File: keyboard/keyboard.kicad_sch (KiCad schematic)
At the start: 4 parts

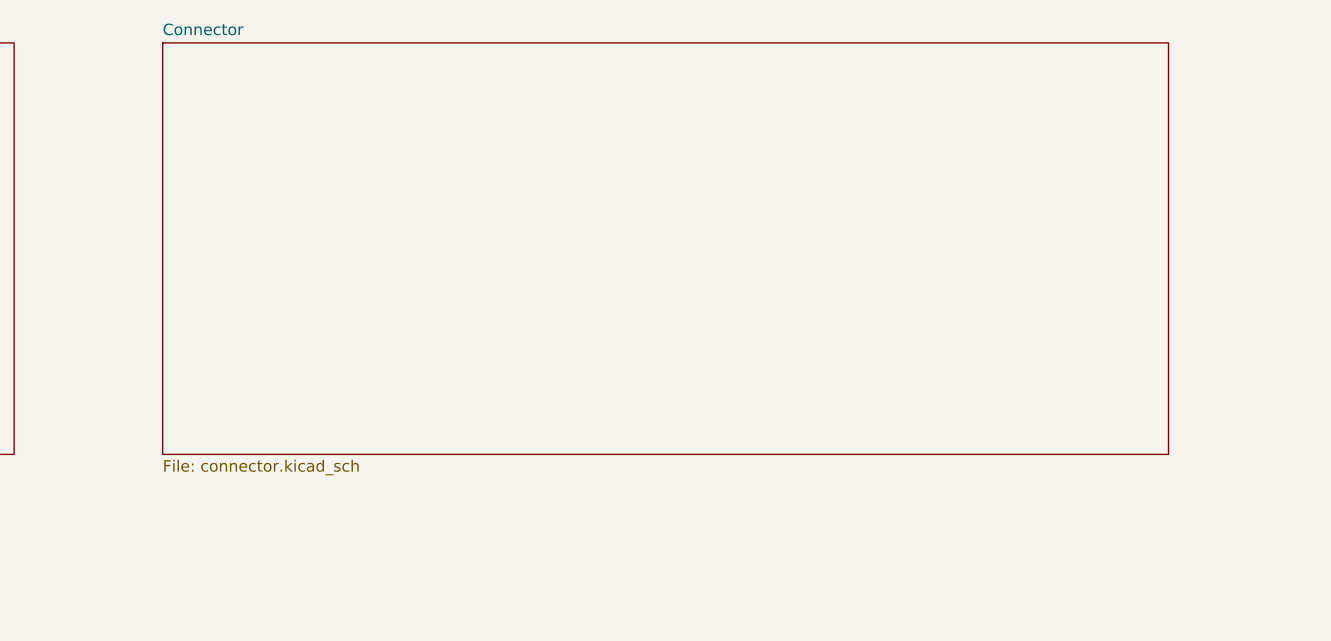
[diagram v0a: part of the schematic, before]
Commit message: Add 3dshapes, footprint library, symbol library, and display mixer board.
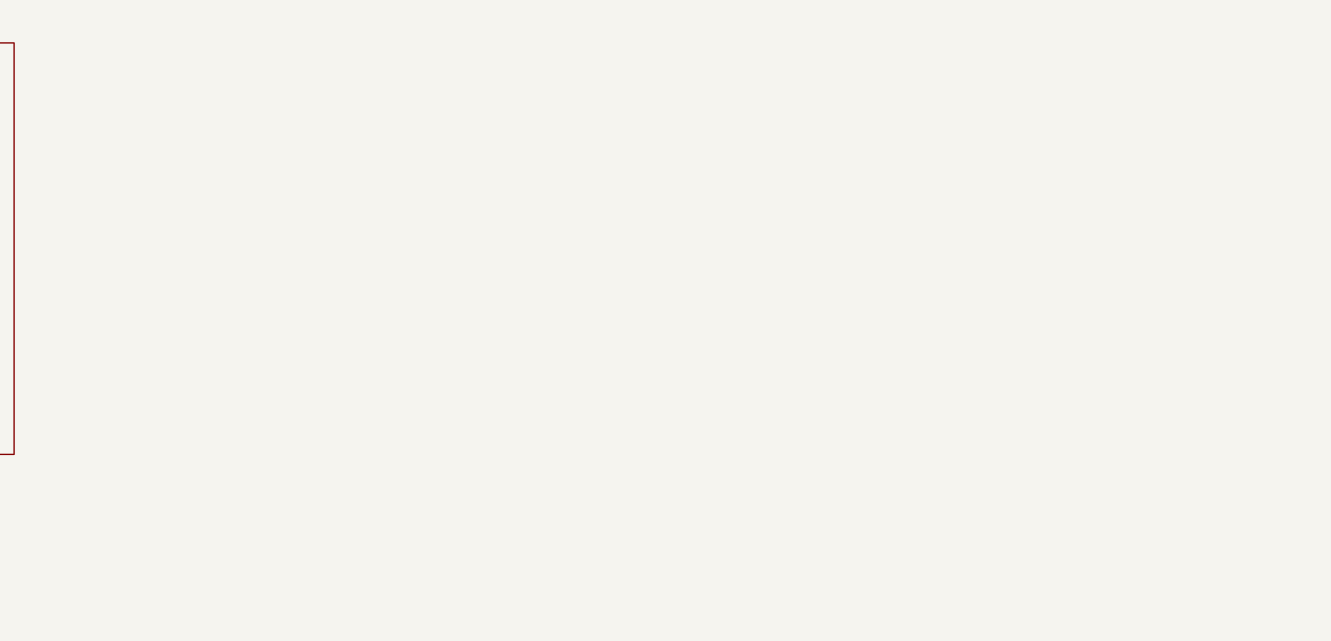
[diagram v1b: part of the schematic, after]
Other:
- removed sheet Connector
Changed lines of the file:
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@@
-	)
-	(sheet
-		(at 127 22.86)
-		(size 111.76 45.72)
-		(exclude_from_sim no)
-		(in_bom yes)
-		(on_board yes)
-		(dnp no)
-		(fields_autoplaced yes)
-		(stroke
-			(width 0.1524)
-			(type solid)
-		)
-		(fill
-			(color 0 0 0 0)
-		)
-		(property "Sheetname" "Connector"
-			(at 127 22.1484 0)
-			(show_name no)
-			(do_not_autoplace no)
-			(effects
-				(font
-					(size 1.27 1.27)
-				)
-				(justify left bottom)
-			)
-		)
-		(property "Sheetfile" "connector.kicad_sch"
-			(at 127 69.1646 0)
-			(show_name no)
-			(do_not_autoplace no)
-			(effects
-				(font
-					(size 1.27 1.27)
-				)
-				(justify left top)
-			)
-		)
-		(instances
-			(project "keyboard"
-				(path "/a799be60-b82b-4047-8bd5-a0d140128afd"
-					(page "3")
-				)
-			)
-		)
 	)
 	(sheet

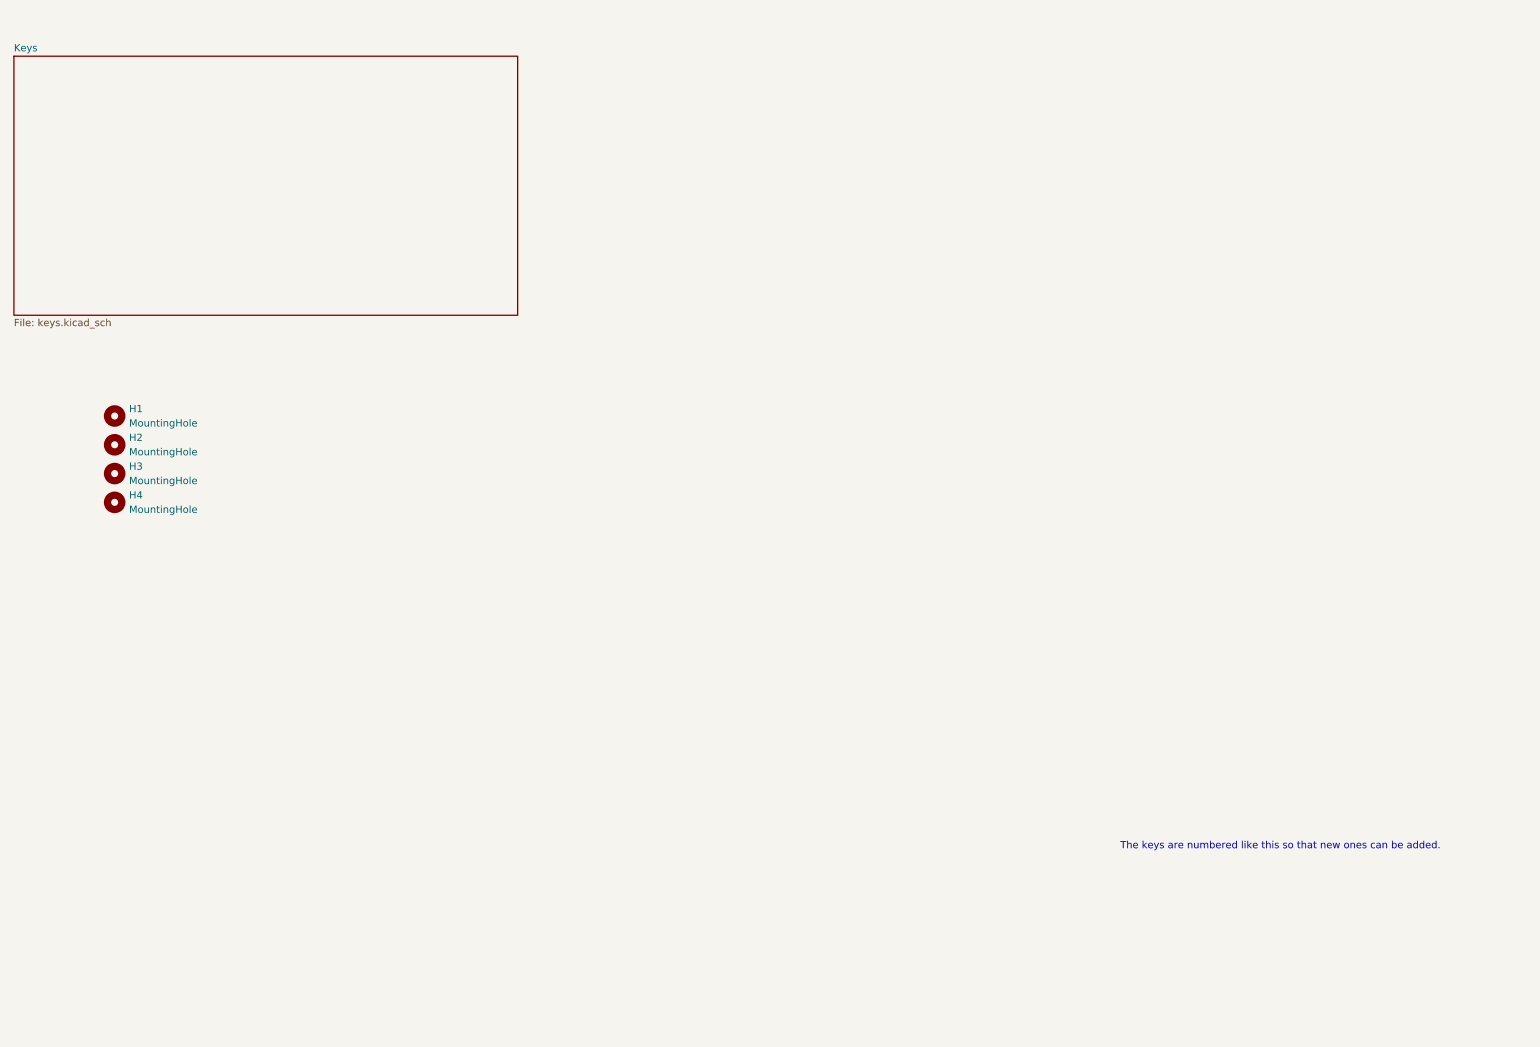
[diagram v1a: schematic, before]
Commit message: Move main connector on display mixer and consolidate keyboard to single sheet.
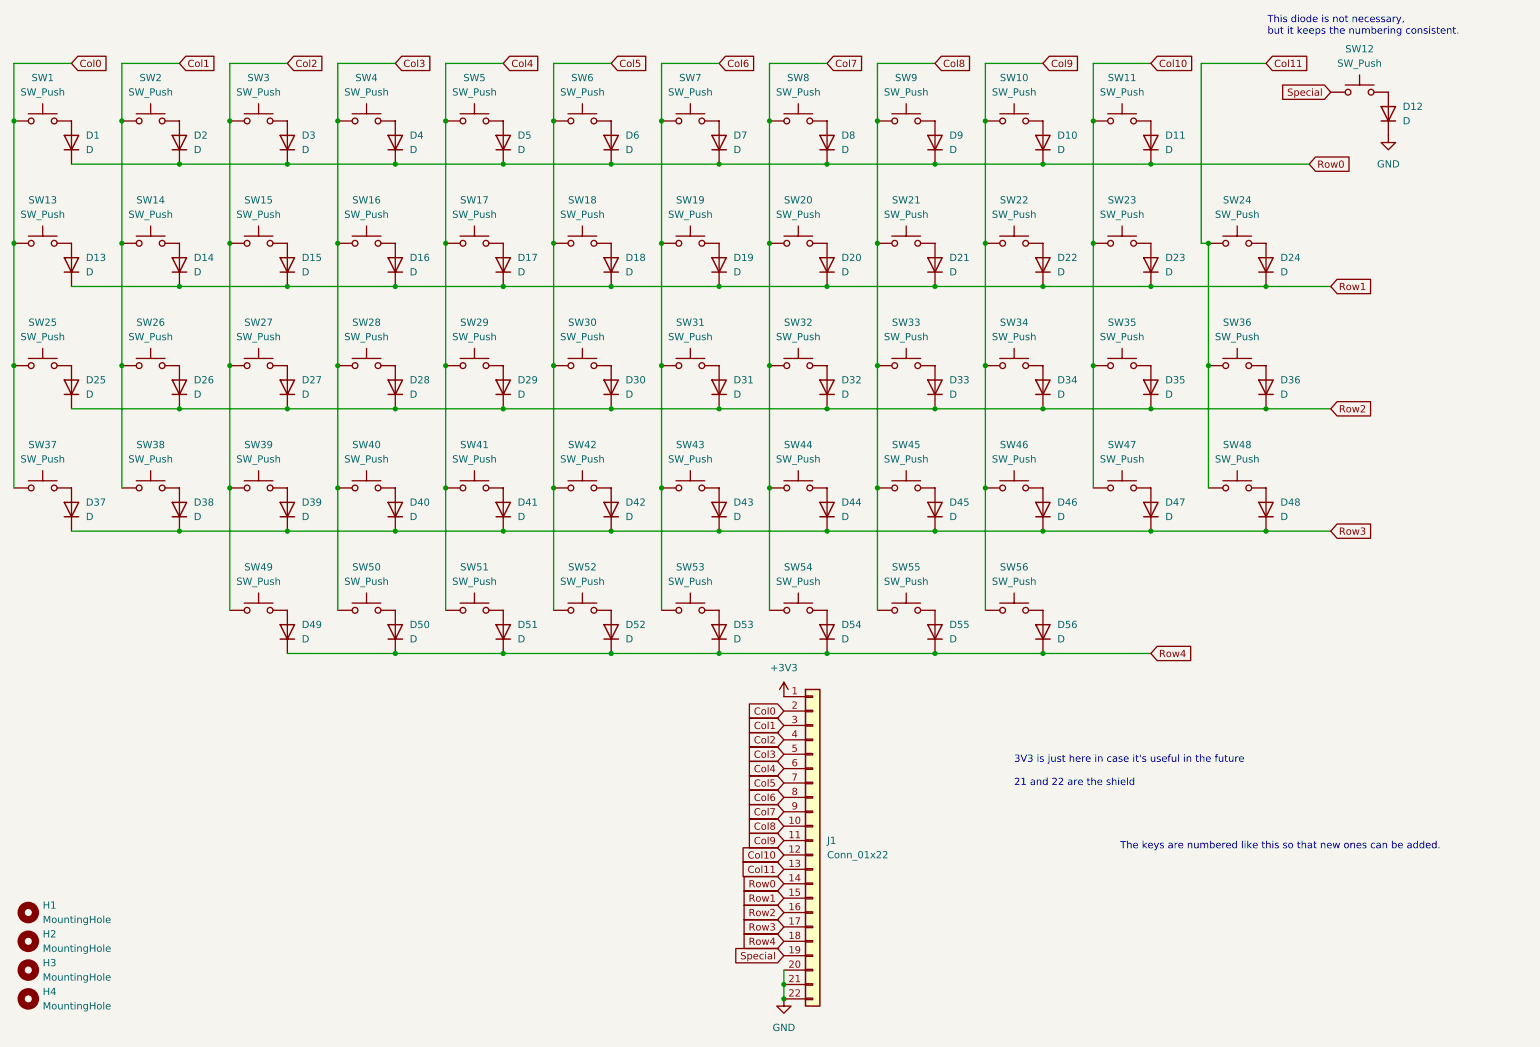
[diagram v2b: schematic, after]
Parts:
- added D1, D10, D11, D12, D13, D14, D15, D16, D17, D18, D19, D2, D20, D21, D22, D23, D24, D25, D26, D27, D28, D29, D3, D30, D31, D32, D33, D34, D35, D36, D37, D38, D39, D4, D40, D41, D42, D43, D44, D45, D46, D47, D48, D49, D5, D50, D51, D52, D53, D54, D55, D56, D6, D7, D8, D9: D, Diode_SMD:D_0402_1005Metric, symbol Device:D
- added J1: Conn_01x22, kirdos:JUSHOU_AFC07-S20FCC-00-FPC-SMD_0.5P, symbol Connector_Generic:Conn_01x22
- added SW1, SW10, SW11, SW12, SW13, SW14, SW15, SW16, SW17, SW18, SW19, SW2, SW20, SW21, SW22, SW23, SW24, SW25, SW26, SW27, SW28, SW29, SW3, SW30, SW31, SW32, SW33, SW34, SW35, SW36, SW37, SW38, SW39, SW4, SW40, SW41, SW42, SW43, SW44, SW45, SW46, SW47, SW48, SW49, SW5, SW50, SW51, SW52, SW53, SW54, SW55, SW56, SW6, SW7, SW8, SW9: SW_Push, PCM_Switch_Keyboard_Kailh:SW_Kailh_Choc_V2, symbol Switch:SW_Push
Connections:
- new net: D18.2 (A), SW18.2
- new net: D52.2 (A), SW52.2
- new net: D19.2 (A), SW19.2
- new net: D22.2 (A), SW22.2
- new net: D26.2 (A), SW26.2
- new net: D48.2 (A), SW48.2
- new net: D17.2 (A), SW17.2
- new net: D47.2 (A), SW47.2
- new net: D28.2 (A), SW28.2
- new net: D40.2 (A), SW40.2
- new net: D50.2 (A), SW50.2
- new net: D33.2 (A), SW33.2
- new net: D45.2 (A), SW45.2
- new net: D41.2 (A), SW41.2
- new net: D44.2 (A), SW44.2
- new net: D56.2 (A), SW56.2
- new net: D38.2 (A), SW38.2
- new net: D10.2 (A), SW10.2
- new net: D12.2 (A), SW12.2
- new net: D5.2 (A), SW5.2
- new net: D21.2 (A), SW21.2
- new net: D35.2 (A), SW35.2
- new net: D46.2 (A), SW46.2
- new net: D11.2 (A), SW11.2
- new net: D49.2 (A), SW49.2
- new net: D30.2 (A), SW30.2
- new net: D37.2 (A), SW37.2
- new net: D16.2 (A), SW16.2
- new net: D55.2 (A), SW55.2
- new net: D3.2 (A), SW3.2
- new net: D23.2 (A), SW23.2
- new net: D53.2 (A), SW53.2
- new net: D1.2 (A), SW1.2
- new net: D32.2 (A), SW32.2
- new net: D27.2 (A), SW27.2
- new net: D31.2 (A), SW31.2
- new net: D2.2 (A), SW2.2
- new net: D8.2 (A), SW8.2
- new net: D24.2 (A), SW24.2
- new net: D7.2 (A), SW7.2
- new net: D4.2 (A), SW4.2
- new net: D43.2 (A), SW43.2
- new net: D42.2 (A), SW42.2
- new net: D36.2 (A), SW36.2
- new net: D39.2 (A), SW39.2
- new net: D51.2 (A), SW51.2
- new net: D9.2 (A), SW9.2
- new net: D54.2 (A), SW54.2
- new net: D13.2 (A), SW13.2
- new net: D34.2 (A), SW34.2
- new net: D6.2 (A), SW6.2
- new net: D14.2 (A), SW14.2
- new net: D20.2 (A), SW20.2
- new net: D25.2 (A), SW25.2
- new net: D29.2 (A), SW29.2
- new net: D15.2 (A), SW15.2
- new net +3V3: J1.1 (Pin_1)
- new net Col0: J1.2 (Pin_2), SW1.1, SW13.1, SW25.1, SW37.1
- new net Col1: J1.3 (Pin_3), SW14.1, SW2.1, SW26.1, SW38.1
- new net Col10: J1.12 (Pin_12), SW11.1, SW23.1, SW35.1, SW47.1
- new net Col11: J1.13 (Pin_13), SW24.1, SW36.1, SW48.1
- new net Col2: J1.4 (Pin_4), SW15.1, SW27.1, SW3.1, SW39.1, SW49.1
- new net Col3: J1.5 (Pin_5), SW16.1, SW28.1, SW4.1, SW40.1, SW50.1
- new net Col4: J1.6 (Pin_6), SW17.1, SW29.1, SW41.1, SW5.1, SW51.1
- new net Col5: J1.7 (Pin_7), SW18.1, SW30.1, SW42.1, SW52.1, SW6.1
- new net Col6: J1.8 (Pin_8), SW19.1, SW31.1, SW43.1, SW53.1, SW7.1
- new net Col7: J1.9 (Pin_9), SW20.1, SW32.1, SW44.1, SW54.1, SW8.1
- new net Col8: J1.10 (Pin_10), SW21.1, SW33.1, SW45.1, SW55.1, SW9.1
- new net Col9: J1.11 (Pin_11), SW10.1, SW22.1, SW34.1, SW46.1, SW56.1
- new net GND: D12.1 (K), J1.20 (Pin_20), J1.21 (Pin_21), J1.22 (Pin_22)
- new net Row0: D1.1 (K), D10.1 (K), D11.1 (K), D2.1 (K), D3.1 (K), D4.1 (K), D5.1 (K), D6.1 (K), D7.1 (K), D8.1 (K), D9.1 (K), J1.14 (Pin_14)
- new net Row1: D13.1 (K), D14.1 (K), D15.1 (K), D16.1 (K), D17.1 (K), D18.1 (K), D19.1 (K), D20.1 (K), D21.1 (K), D22.1 (K), D23.1 (K), D24.1 (K), J1.15 (Pin_15)
- new net Row2: D25.1 (K), D26.1 (K), D27.1 (K), D28.1 (K), D29.1 (K), D30.1 (K), D31.1 (K), D32.1 (K), D33.1 (K), D34.1 (K), D35.1 (K), D36.1 (K), J1.16 (Pin_16)
- new net Row3: D37.1 (K), D38.1 (K), D39.1 (K), D40.1 (K), D41.1 (K), D42.1 (K), D43.1 (K), D44.1 (K), D45.1 (K), D46.1 (K), D47.1 (K), D48.1 (K), J1.17 (Pin_17)
- new net Row4: D49.1 (K), D50.1 (K), D51.1 (K), D52.1 (K), D53.1 (K), D54.1 (K), D55.1 (K), D56.1 (K), J1.18 (Pin_18)
- new net Special: J1.19 (Pin_19), SW12.1
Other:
- removed sheet Keys
- note added: "3V3 is just here in case it's useful in the future 21 and 22 are the shield"
- note added: "This diode is not necessary, but it keeps the numbering consistent."
